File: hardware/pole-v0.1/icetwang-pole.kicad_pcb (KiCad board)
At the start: 2 copper layers, 48 x 61 mm, 80 parts, among them J1 COMM5V, J10 RGB_LED, J11 5V, J12 5V, J2 COMMGND, J3 RJ45, J4 COMM5V, J5 COMMGND, J6 RJ45, J7 RGB_LED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

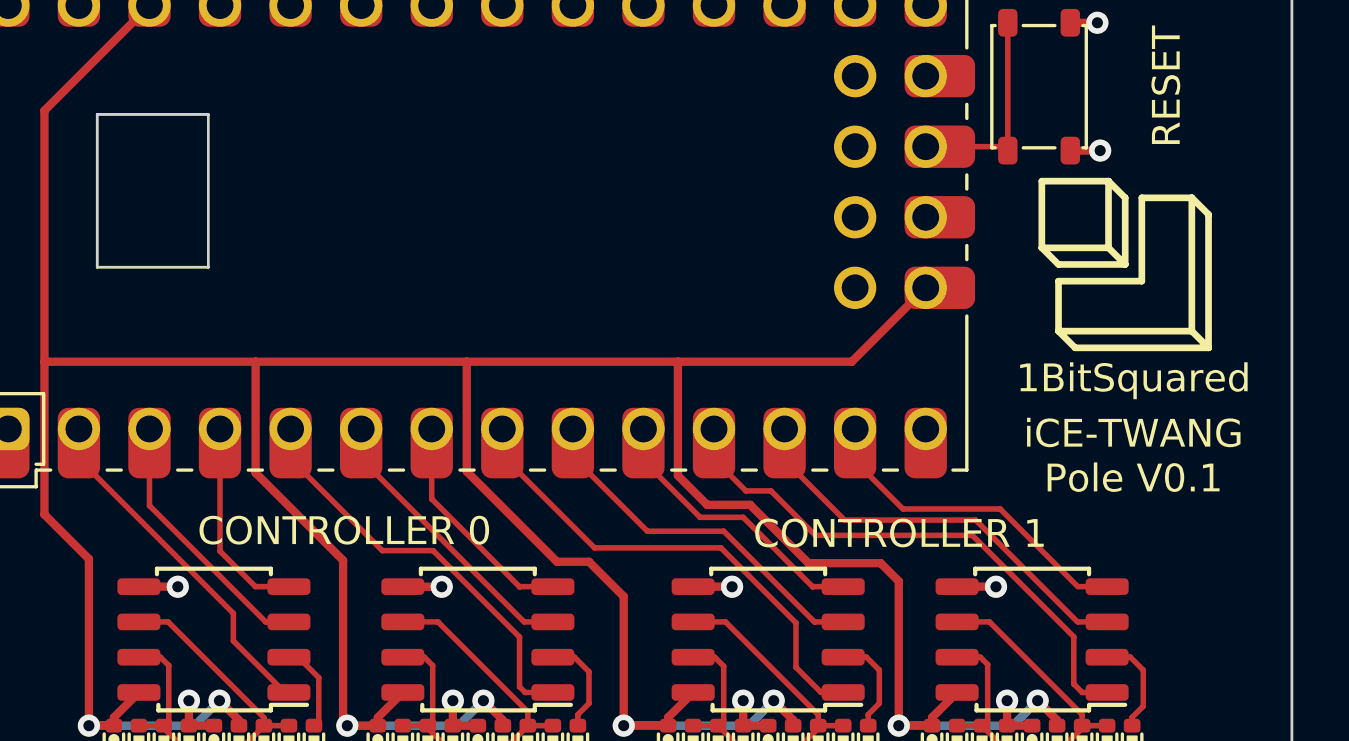
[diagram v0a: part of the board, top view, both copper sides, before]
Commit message: Swapped to NULL logos and added pdf schematics.
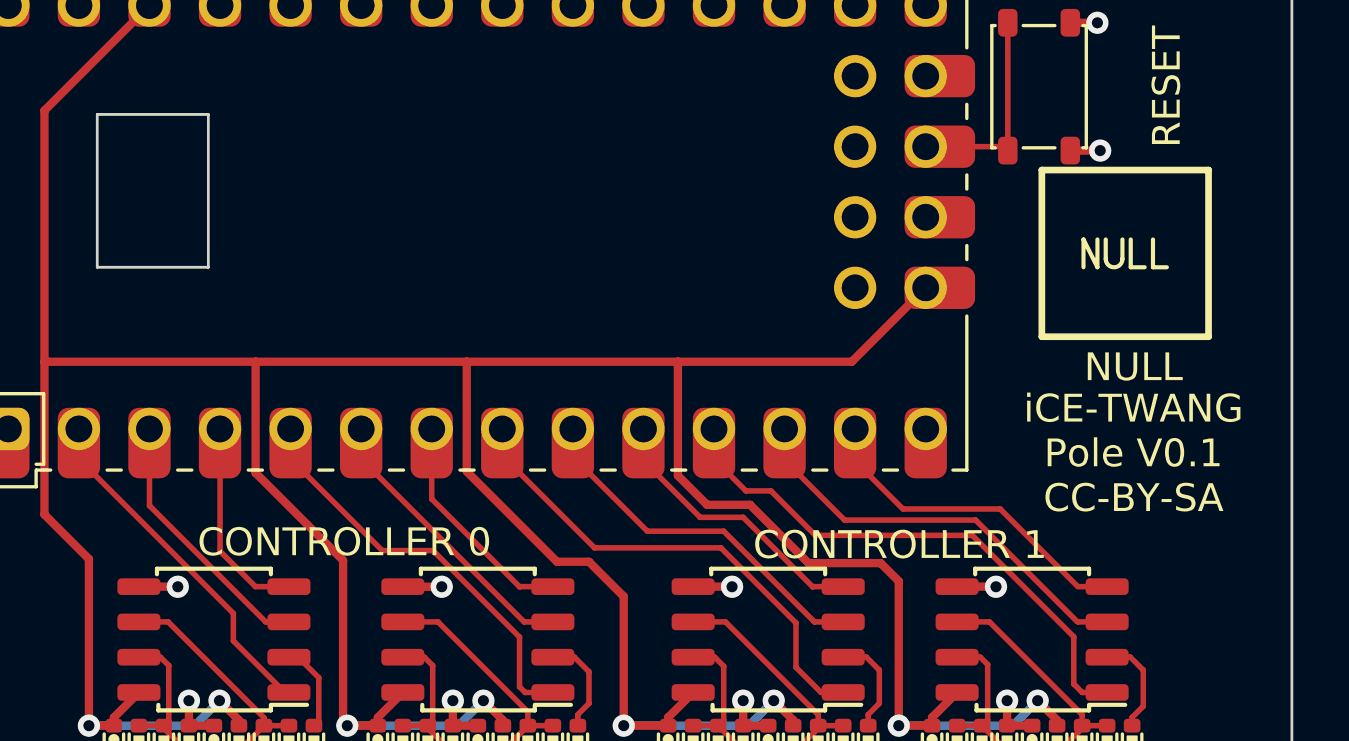
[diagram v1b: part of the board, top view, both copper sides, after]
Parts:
- REF**: value 1b2_Logo_SilkS_6mm -> null_Logo_SilkS_6mm; footprint pkl_logos:1b2_Logo_SilkS_6mm -> pkl_logos:null_Logo_SilkS_6mm
- REF**: value 1b2_Logo_SilkS_10mm -> null_Logo_SilkS_10mm; footprint pkl_logos:1b2_Logo_SilkS_10mm -> pkl_logos:null_Logo_SilkS_10mm
- moved REF** 0.40 mm to (62.0, 45.0)
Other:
- board text added: "NULL"
- board text added: "iCE-TWANG Pole V0.1 CC-BY-SA"
- board text removed: "1BitSquared"
- board text removed: "iCE-TWANG Pole V0.1"
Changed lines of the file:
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@@
     )
   )
-  (footprint "pkl_logos:1b2_Logo_SilkS_6mm" (layer "F.Cu")
-    (at 62 45.4)
-    (descr "1BitSquared Logo, Silk Screen, 6mm")
-    (tags "logo symbol 1bitsquared 1b2")
+  (footprint "pkl_logos:null_Logo_SilkS_6mm" (layer "F.Cu")
+    (at 62 45)
+    (descr "NULL Logo, Silk Screen, 6mm")
+    (tags "logo symbol null")
     (attr exclude_from_pos_files exclude_from_bom)
     (fp_text reference "REF**" (at 0 -4) (layer "F.SilkS") hide
       (effects (font (size 1 1) (thickness 0.15)))
     )
-    (fp_text value "1b2_Logo_SilkS_6mm" (at 0 4) (layer "F.Fab") hide
-      (effects (font (size 1 1) (thickness 0.15)))
-    )
-    (fp_line (start 2.4 2.4) (end -2.4 2.4) (layer "F.SilkS") (width 0.24))
-    (fp_line (start 3 3) (end -1.8 3) (layer "F.SilkS") (width 0.24))
-    (fp_line (start 0 -2.4) (end 0 0) (layer "F.SilkS") (width 0.24))
-    (fp_line (start 2.4 2.4) (end 3 3) (layer "F.SilkS") (width 0.24))
-    (fp_line (start -0.6 -3) (end 0 -2.4) (layer "F.SilkS") (width 0.24))
-    (fp_line (start -2.4 0) (end -3 -0.6) (layer "F.SilkS") (width 0.24))
-    (fp_line (start -3 -3) (end -0.6 -3) (layer "F.SilkS") (width 0.24))
-    (fp_line (start -0.6 -0.6) (end -3 -0.6) (layer "F.SilkS") (width 0.24))
-    (fp_line (start 0 0) (end -2.4 0) (layer "F.SilkS") (width 0.24))
-    (fp_line (start 2.4 -2.4) (end 2.4 2.4) (layer "F.SilkS") (width 0.24))
-    (fp_line (start 3 -1.8) (end 3 3) (layer "F.SilkS") (width 0.24))
-    (fp_line (start 2.4 -2.4) (end 3 -1.8) (layer "F.SilkS") (width 0.24))
-    (fp_line (start -0.6 -3) (end -0.6 -0.6) (layer "F.SilkS") (width 0.24))
-    (fp_line (start -3 -0.6) (end -3 -3) (layer "F.SilkS") (width 0.24))
-    (fp_line (start -2.4 0.6) (end 0.6 0.6) (layer "F.SilkS") (width 0.24))
-    (fp_line (start -2.4 2.4) (end -2.4 0.6) (layer "F.SilkS") (width 0.24))
-    (fp_line (start 0.6 -2.4) (end 2.4 -2.4) (layer "F.SilkS") (width 0.24))
-    (fp_line (start -0.6 -0.6) (end 0 0) (layer "F.SilkS") (width 0.24))
-    (fp_line (start 0.6 0.6) (end 0.6 -2.4) (layer "F.SilkS") (width 0.24))
-    (fp_line (start -1.8 3) (end -2.4 2.4) (layer "F.SilkS") (width 0.24))
+    (fp_text value "null_Logo_SilkS_6mm" (at 0 4) (layer "F.Fab") hide
+      (effects (font (size 1 1) (thickness 0.15)))
+    )
+    (fp_line (start -3 -3) (end -3 3) (layer "F.SilkS") (width 0.24))
+    (fp_line (start -0.7 -0.5) (end -0.7 0.2) (layer "F.SilkS") (width 0.15))
+    (fp_line (start 0.2 0.5) (end 0.7 0.5) (layer "F.SilkS") (width 0.15))
+    (fp_line (start -1.5 0.5) (end -1.5 -0.5) (layer "F.SilkS") (width 0.15))
+    (fp_line (start -1 0.5) (end -1 -0.5) (layer "F.SilkS") (width 0.15))
+    (fp_line (start 3 -3) (end -3 -3) (layer "F.SilkS") (width 0.24))
+    (fp_line (start 0.2 -0.5) (end 0.2 0.5) (layer "F.SilkS") (width 0.15))
+    (fp_line (start -3 3) (end 3 3) (layer "F.SilkS") (width 0.24))
+    (fp_line (start 1 -0.5) (end 1 0.5) (layer "F.SilkS") (width 0.15))
+    (fp_line (start 3 -3) (end 3 3) (layer "F.SilkS") (width 0.24))
+    (fp_line (start -0.1 0.2) (end -0.1 -0.5) (layer "F.SilkS") (width 0.15))
+    (fp_line (start -1.5 -0.5) (end -1 0.5) (layer "F.SilkS") (width 0.15))
+    (fp_line (start 1 0.5) (end 1.5 0.5) (layer "F.SilkS") (width 0.15))
+    (fp_arc (start -0.4 0.2) (end -0.7 0.2) (angle -180) (layer "F.SilkS") (width 0.15))
   )
   (footprint "pkl_dipol:R_0402" (layer "F.Cu")
@@
     )
   )
-  (footprint "pkl_logos:1b2_Logo_SilkS_10mm" (layer "B.Cu")
+  (footprint "pkl_logos:null_Logo_SilkS_10mm" (layer "B.Cu")
     (at 45.2 42.5 180)
-    (descr "1BitSquared Logo, Silk Screen, 10mm")
-    (tags "logo symbol 1bitsquared 1b2")
+    (descr "NULL Logo, Silk Screen, 10mm")
+    (tags "logo symbol null")
     (attr exclude_from_pos_files exclude_from_bom)
     (fp_text reference "REF**" (at 0 6) (layer "B.SilkS") hide
       (effects (font (size 1 1) (thickness 0.15)) (justify mirror))
     )
-    (fp_text value "1b2_Logo_SilkS_10mm" (at 0 -6) (layer "B.Fab") hide
+    (fp_text value "null_Logo_SilkS_10mm" (at 0 -6) (layer "B.Fab") hide
       (effects (font (size 1 1) (thickness 0.15)) (justify mirror))
     )
-    (fp_line (start -5 1) (end -1 1) (layer "B.SilkS") (width 0.4))
-    (fp_line (start 0 4) (end 0 0) (layer "B.SilkS") (width 0.4))
-    (fp_line (start 1 -1) (end -4 -1) (layer "B.SilkS") (width 0.4))
-    (fp_line (start 4 -4) (end 4 4) (layer "B.SilkS") (width 0.4))
-    (fp_line (start 1 4) (end 1 -1) (layer "B.SilkS") (width 0.4))
-    (fp_line (start 4 4) (end 5 3) (layer "B.SilkS") (width 0.4))
-    (fp_line (start 5 3) (end 5 -5) (layer "B.SilkS") (width 0.4))
-    (fp_line (start -5 1) (end -4 0) (layer "B.SilkS") (width 0.4))
-    (fp_line (start -4 0) (end 0 0) (layer "B.SilkS") (width 0.4))
-    (fp_line (start -1 5) (end -5 5) (layer "B.SilkS") (width 0.4))
-    (fp_line (start 5 -5) (end 4 -4) (layer "B.SilkS") (width 0.4))
-    (fp_line (start 0 0) (end -1 1) (layer "B.SilkS") (width 0.4))
-    (fp_line (start -4 -1) (end -4 -4) (layer "B.SilkS") (width 0.4))
-    (fp_line (start -3 -5) (end 5 -5) (layer "B.SilkS") (width 0.4))
-    (fp_line (start -4 -4) (end 4 -4) (layer "B.SilkS") (width 0.4))
-    (fp_line (start 4 4) (end 1 4) (layer "B.SilkS") (width 0.4))
-    (fp_line (start -5 5) (end -5 1) (layer "B.SilkS") (width 0.4))
-    (fp_line (start -1 1) (end -1 5) (layer "B.SilkS") (width 0.4))
-    (fp_line (start -1 5) (end 0 4) (layer "B.SilkS") (width 0.4))
-    (fp_line (start -4 -4) (end -3 -5) (layer "B.SilkS") (width 0.4))
+    (fp_line (start -0.1 0.5) (end -0.1 -0.2) (layer "B.SilkS") (width 0.15))
+    (fp_line (start -1 -0.5) (end -1 0.5) (layer "B.SilkS") (width 0.15))
+    (fp_line (start -0.7 0.5) (end -0.7 -0.2) (layer "B.SilkS") (width 0.15))
+    (fp_line (start -1.5 -0.5) (end -1.5 0.5) (layer "B.SilkS") (width 0.15))
+    (fp_line (start 5 5) (end -5 5) (layer "B.SilkS") (width 0.4))
+    (fp_line (start 0.2 -0.5) (end 0.7 -0.5) (layer "B.SilkS") (width 0.15))
+    (fp_line (start 1 -0.5) (end 1.5 -0.5) (layer "B.SilkS") (width 0.15))
+    (fp_line (start -5 5) (end -5 -5) (layer "B.SilkS") (width 0.4))
+    (fp_line (start 5 5) (end 5 -5) (layer "B.SilkS") (width 0.4))
+    (fp_line (start 1 0.5) (end 1 -0.5) (layer "B.SilkS") (width 0.15))
+    (fp_line (start -1.5 0.5) (end -1 -0.5) (layer "B.SilkS") (width 0.15))
+    (fp_line (start 0.2 0.5) (end 0.2 -0.5) (layer "B.SilkS") (width 0.15))
+    (fp_line (start -5 -5) (end 5 -5) (layer "B.SilkS") (width 0.4))
+    (fp_arc (start -0.4 -0.2) (end -0.7 -0.2) (angle 180) (layer "B.SilkS") (width 0.15))
   )
   (footprint "pkl_jumpers:J_NC_0603_40" (layer "B.Cu")
@@
   (gr_line (start 20 79) (end 20 22) (layer "Edge.Cuts") (width 0.1))
   (gr_rect (start 25 40) (end 29 45.5) (layer "Edge.Cuts") (width 0.1) (fill none))
-  (gr_text "iCE-TWANG\nPole\nV0.1" (at 32.6 40.6) (layer "B.SilkS")
+  (gr_text "iCE-TWANG\nPole\nV0.1\nCC-BY-SA" (at 32.8 42.8) (layer "B.SilkS")
     (effects (font (size 1.5 1.5) (thickness 0.3)) (justify mirror))
   )
@@
     (effects (font (size 1 1) (thickness 0.15)) (justify mirror))
   )
-  (gr_text "1BitSquared" (at 44.7 49.1) (layer "B.SilkS")
+  (gr_text "NULL" (at 44.7 49.1) (layer "B.SilkS")
     (effects (font (size 1.5 1.5) (thickness 0.3)) (justify mirror))
   )
@@
     (effects (font (size 1 1) (thickness 0.15)))
   )
-  (gr_text "CONTROLLER 0" (at 33.9 55) (layer "F.SilkS")
+  (gr_text "CONTROLLER 0" (at 33.9 55.4) (layer "F.SilkS")
     (effects (font (size 1 1) (thickness 0.15)))
   )
@@
     (effects (font (size 1 1) (thickness 0.15)))
   )
-  (gr_text "iCE-TWANG\nPole V0.1" (at 62.3 52.3) (layer "F.SilkS")
+  (gr_text "iCE-TWANG\nPole V0.1\nCC-BY-SA" (at 62.3 52.2) (layer "F.SilkS")
     (effects (font (size 1 1) (thickness 0.15)))
   )
@@
     (effects (font (size 1 1) (thickness 0.15)))
   )
-  (gr_text "CONTROLLER 1" (at 53.9 55.1) (layer "F.SilkS")
+  (gr_text "CONTROLLER 1" (at 53.9 55.5) (layer "F.SilkS")
     (effects (font (size 1 1) (thickness 0.15)))
   )
@@
     (effects (font (size 1 1) (thickness 0.15)))
   )
-  (gr_text "1BitSquared" (at 62.3 49.5) (layer "F.SilkS")
+  (gr_text "NULL" (at 62.3 49.1) (layer "F.SilkS")
     (effects (font (size 1 1) (thickness 0.15)))
   )
